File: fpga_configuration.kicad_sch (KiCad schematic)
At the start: 53 parts, among them IC1 ECP5-BGA256, J10 TC_SWD, J6 MCU_SWD, U6 ATSAMD11, U7 W25Q32JVSS

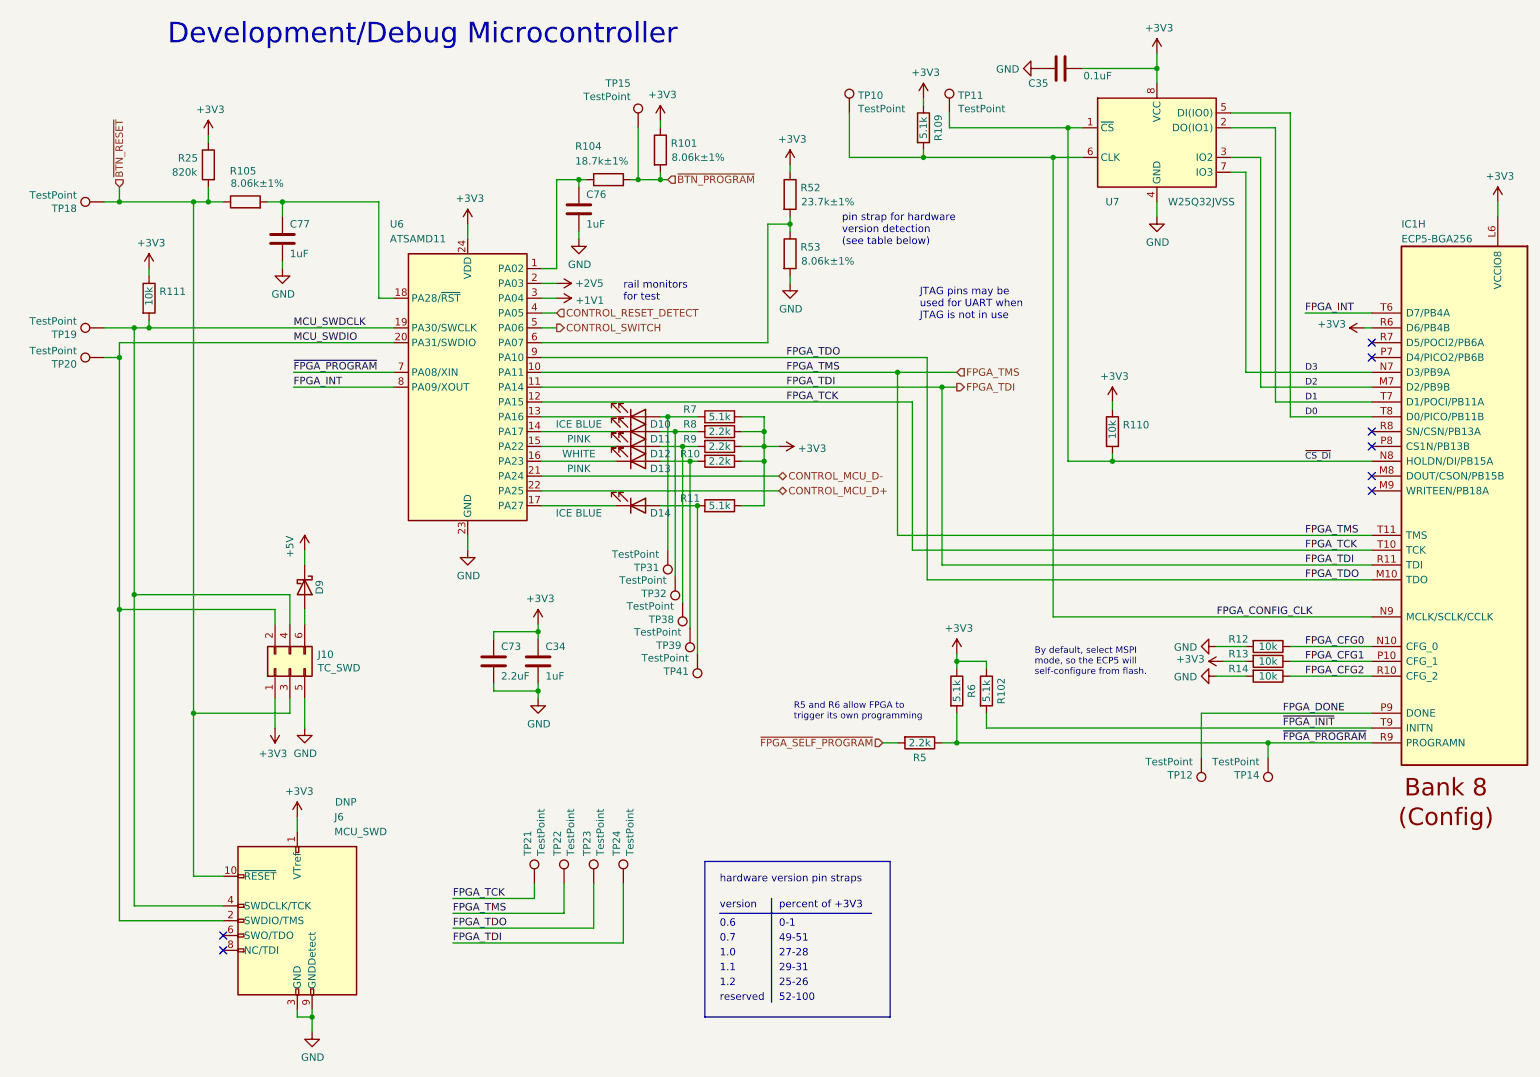
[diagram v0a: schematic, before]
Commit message: Connect FPGA_DONE and FPGA_INIT to microcontroller
Also pull FPGA_INIT (INITN) down instead of up. This prevents the FPGA
from self-configuring at start-up until the microcontroller drives the
signal high.

Connecting these signals give the microcontroller better control and
monitoring of the FPGA's configuration process.

To make room for these signals, the +1V1 and +2V5 measurement
connections are removed from the microcontroller.
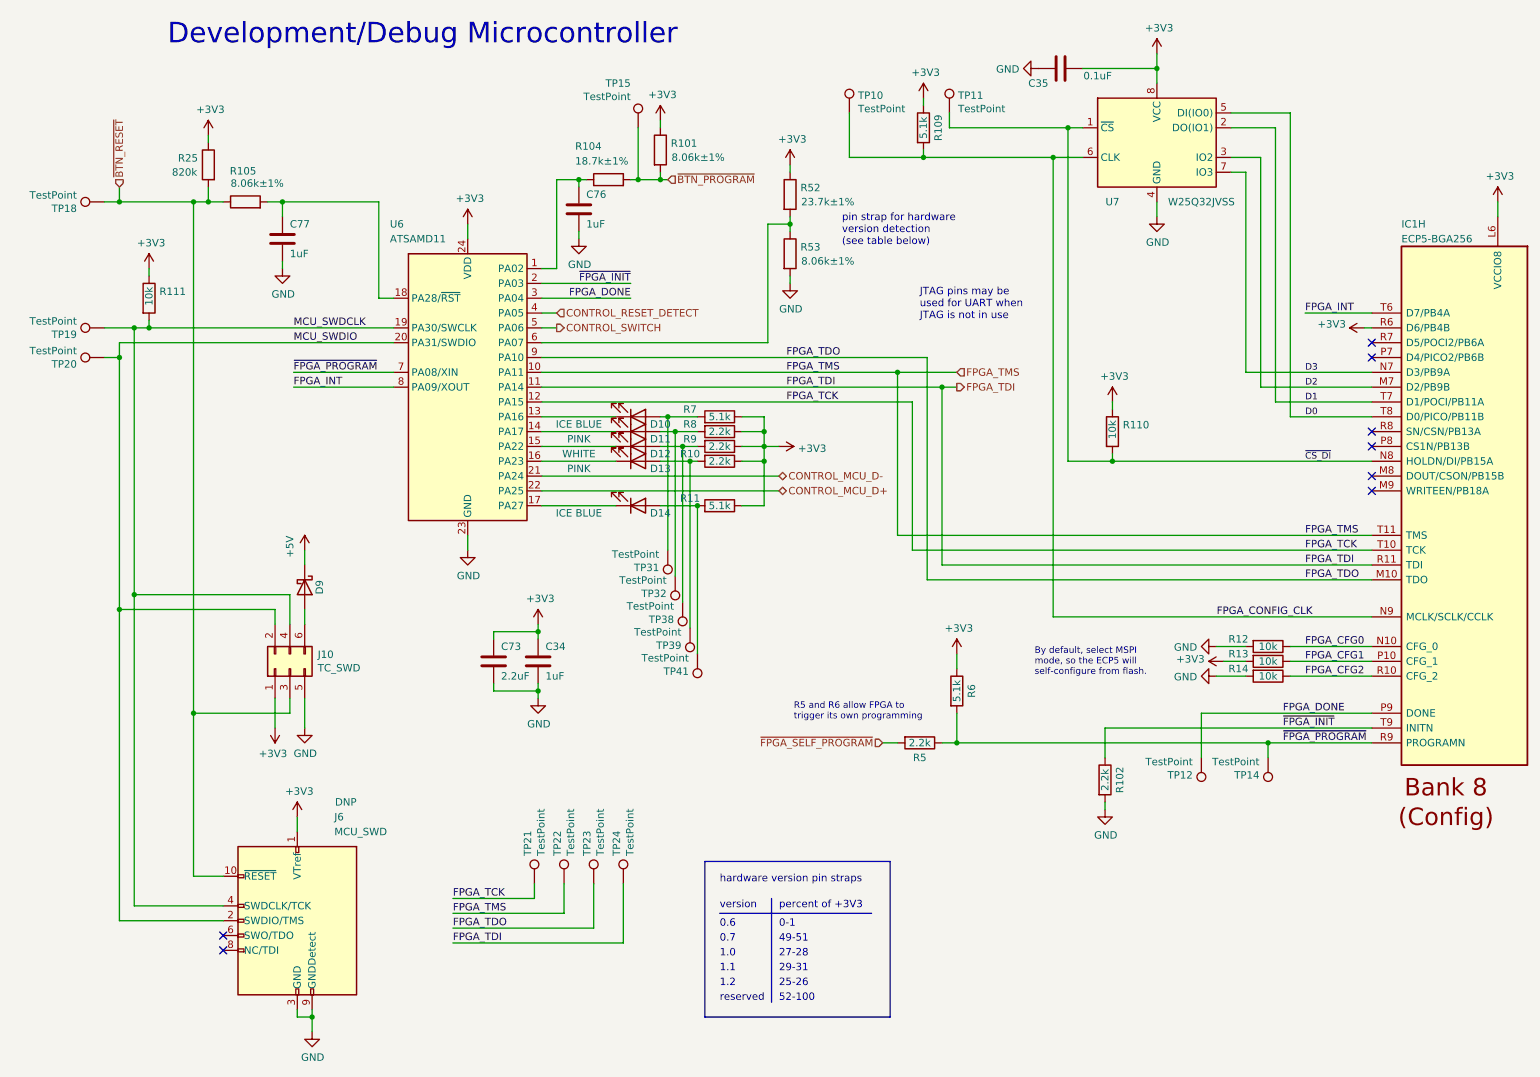
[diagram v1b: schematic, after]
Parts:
- R102: value 5.1k -> 2.2k; Part Number RC0402JR-075K1L -> RC0402JR-072K2L
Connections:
- net +1V1 is gone; now on net FPGA_DONE: U6.3 (PA04)
- net +2V5 is gone; now on net ~{FPGA_INIT}: U6.2 (PA03)
- net +3V3: no longer R102.1
- net GND: now also R102.2
- net ~{FPGA_INIT}: now also R102.1; no longer R102.2
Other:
- note removed: "rail monitors for test"
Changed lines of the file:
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@@
   (junction (at 33.02 74.93) (diameter 0) (color 0 0 0 0)
-  )
-  (junction (at 176.53 127) (diameter 0) (color 0 0 0 0)
   )
   (junction (at 121.92 44.45) (diameter 0) (color 0 0 0 0)
@@
     (stroke (width 0) (type default) (color 0 0 0 0))
   )
+  (wire (pts (xy 247.65 138.43) (xy 201.93 138.43))
+    (stroke (width 0) (type default) (color 0 0 0 0))
+  )
   (wire (pts (xy 107.95 69.85) (xy 105.41 69.85))
     (stroke (width 0) (type default) (color 0 0 0 0))
@@
     (stroke (width 0) (type default) (color 0 0 0 0))
   )
-  (wire (pts (xy 107.95 64.77) (xy 105.41 64.77))
+  (wire (pts (xy 120.65 64.77) (xy 105.41 64.77))
     (stroke (width 0) (type default) (color 0 0 0 0))
   )
@@
     (stroke (width 0) (type default) (color 0 0 0 0))
   )
-  (wire (pts (xy 176.53 125.73) (xy 176.53 127))
+  (wire (pts (xy 176.53 125.73) (xy 176.53 128.27))
     (stroke (width 0) (type default) (color 0 0 0 0))
   )
@@
     (stroke (width 0) (type default) (color 0 0 0 0))
   )
-  (wire (pts (xy 105.41 62.23) (xy 107.95 62.23))
+  (wire (pts (xy 105.41 62.23) (xy 120.65 62.23))
     (stroke (width 0) (type default) (color 0 0 0 0))
   )
@@
     (stroke (width 0) (type default) (color 0 0 0 0))
   )
+  (wire (pts (xy 201.93 151.13) (xy 201.93 152.4))
+    (stroke (width 0) (type default) (color 0 0 0 0))
+  )
   (wire (pts (xy 121.92 35.56) (xy 121.92 44.45))
     (stroke (width 0) (type default) (color 0 0 0 0))
@@
     (stroke (width 0) (type default) (color 0 0 0 0))
   )
-  (wire (pts (xy 181.61 135.89) (xy 181.61 138.43))
-    (stroke (width 0) (type default) (color 0 0 0 0))
-  )
   (wire (pts (xy 107.95 44.45) (xy 107.95 59.69))
     (stroke (width 0) (type default) (color 0 0 0 0))
@@
     (stroke (width 0) (type default) (color 0 0 0 0))
   )
-  (wire (pts (xy 176.53 127) (xy 176.53 128.27))
-    (stroke (width 0) (type default) (color 0 0 0 0))
-  )
   (wire (pts (xy 127 85.09) (xy 132.08 85.09))
     (stroke (width 0) (type default) (color 0 0 0 0))
@@
     (stroke (width 0) (type default) (color 0 0 0 0))
   )
-  (wire (pts (xy 247.65 138.43) (xy 181.61 138.43))
-    (stroke (width 0) (type default) (color 0 0 0 0))
-  )
   (wire (pts (xy 147.955 53.34) (xy 147.955 52.07))
     (stroke (width 0) (type default) (color 0 0 0 0))
   )
-  (wire (pts (xy 181.61 127) (xy 181.61 128.27))
-    (stroke (width 0) (type default) (color 0 0 0 0))
-  )
   (wire (pts (xy 109.22 170.18) (xy 90.17 170.18))
     (stroke (width 0) (type default) (color 0 0 0 0))
@@
     (stroke (width 0) (type default) (color 0 0 0 0))
   )
-  (wire (pts (xy 176.53 127) (xy 181.61 127))
-    (stroke (width 0) (type default) (color 0 0 0 0))
-  )
   (wire (pts (xy 63.5 187.96) (xy 66.04 187.96))
     (stroke (width 0) (type default) (color 0 0 0 0))
@@
   )
   (wire (pts (xy 50.8 48.26) (xy 48.26 48.26))
+    (stroke (width 0) (type default) (color 0 0 0 0))
+  )
+  (wire (pts (xy 201.93 138.43) (xy 201.93 143.51))
     (stroke (width 0) (type default) (color 0 0 0 0))
   )
@@
     (effects (font (size 1.27 1.27)) (justify left bottom))
   )
-  (text "rail monitors\nfor test" (at 119.38 65.405 0)
-    (effects (font (size 1.27 1.27)) (justify left bottom))
-  )
   (text "pin strap for hardware\nversion detection\n(see table below)"
     (at 156.845 55.88 0)
@@
     (effects (font (size 1.27 1.27)) (justify left bottom))
   )
+  (label "FPGA_DONE" (at 120.65 64.77 180)
+    (effects (font (size 1.27 1.27)) (justify right bottom))
+  )
   (label "MCU_SWDCLK" (at 62.865 69.85 0)
     (effects (font (size 1.27 1.27)) (justify left bottom))
+  )
+  (label "~{FPGA_INIT}" (at 120.65 62.23 180)
+    (effects (font (size 1.27 1.27)) (justify right bottom))
   )
   (label "FPGA_INT" (at 236.22 67.31 0)
@@
     )
     (property "Datasheet" "" (id 3) (at 146.05 90.17 0)
-      (effects (font (size 1.27 1.27)) hide)
-    )
-    (pin "1")
-  )
-  (symbol (lib_id "power:+1V1") (at 107.95 64.77 270) (unit 1)
-    (in_bom yes) (on_board yes)
-    (property "Reference" "#PWR040" (id 0) (at 104.14 64.77 0)
-      (effects (font (size 1.27 1.27)) hide)
-    )
-    (property "Value" "+1V1" (id 1) (at 111.2012 65.151 90)
-      (effects (font (size 1.27 1.27)) (justify left))
-    )
-    (property "Footprint" "" (id 2) (at 107.95 64.77 0)
-      (effects (font (size 1.27 1.27)) hide)
-    )
-    (property "Datasheet" "" (id 3) (at 107.95 64.77 0)
-      (effects (font (size 1.27 1.27)) hide)
-    )
-    (pin "1")
-  )
-  (symbol (lib_id "power:+2V5") (at 107.95 62.23 270) (unit 1)
-    (in_bom yes) (on_board yes)
-    (property "Reference" "#PWR046" (id 0) (at 104.14 62.23 0)
-      (effects (font (size 1.27 1.27)) hide)
-    )
-    (property "Value" "+2V5" (id 1) (at 111.125 62.23 90)
-      (effects (font (size 1.27 1.27)) (justify left))
-    )
-    (property "Footprint" "" (id 2) (at 107.95 62.23 0)
-      (effects (font (size 1.27 1.27)) hide)
-    )
-    (property "Datasheet" "" (id 3) (at 107.95 62.23 0)
       (effects (font (size 1.27 1.27)) hide)
     )
@@
     (pin "1")
   )
+  (symbol (lib_id "Device:R") (at 201.93 147.32 0) (unit 1)
+    (in_bom yes) (on_board yes)
+    (property "Reference" "R102" (id 0) (at 204.47 147.32 90))
+    (property "Value" "2.2k" (id 1) (at 201.93 147.32 90))
+    (property "Footprint" "Resistor_SMD:R_0402_1005Metric" (id 2) (at 200.152 147.32 90)
+      (effects (font (size 1.27 1.27)) hide)
+    )
+    (property "Datasheet" "~" (id 3) (at 201.93 147.32 0)
+      (effects (font (size 1.27 1.27)) hide)
+    )
+    (property "Part Number" "RC0402JR-072K2L" (id 4) (at 201.93 147.32 0)
+      (effects (font (size 1.27 1.27)) hide)
+    )
+    (property "Substitution" "any equivalent" (id 5) (at 201.93 147.32 0)
+      (effects (font (size 1.27 1.27)) hide)
+    )
+    (property "Description" "RES 2.2K OHM 5% 1/16W 0402" (id 6) (at 201.93 147.32 0)
+      (effects (font (size 1.27 1.27)) hide)
+    )
+    (property "Manufacturer" "Yageo" (id 7) (at 201.93 147.32 0)
+      (effects (font (size 1.27 1.27)) hide)
+    )
+    (pin "1")
+    (pin "2")
+  )
   (symbol (lib_id "Connector:TestPoint") (at 132.08 125.73 180) (unit 1)
     (in_bom no) (on_board yes)
@@
     (pin "2")
   )
+  (symbol (lib_id "power:GND") (at 201.93 152.4 0) (unit 1)
+    (in_bom yes) (on_board yes)
+    (property "Reference" "#PWR0237" (id 0) (at 201.93 158.75 0)
+      (effects (font (size 1.27 1.27)) hide)
+    )
+    (property "Value" "GND" (id 1) (at 202.057 156.7942 0))
+    (property "Footprint" "" (id 2) (at 201.93 152.4 0)
+      (effects (font (size 1.27 1.27)) hide)
+    )
+    (property "Datasheet" "" (id 3) (at 201.93 152.4 0)
+      (effects (font (size 1.27 1.27)) hide)
+    )
+    (pin "1")
+  )
   (symbol (lib_id "Device:R") (at 203.2 87.63 0) (unit 1)
     (in_bom yes) (on_board yes)
@@
     (pin "1")
   )
-  (symbol (lib_id "Device:R") (at 181.61 132.08 0) (unit 1)
-    (in_bom yes) (on_board yes)
-    (property "Reference" "R102" (id 0) (at 184.15 132.08 90))
-    (property "Value" "5.1k" (id 1) (at 181.61 132.08 90))
-    (property "Footprint" "Resistor_SMD:R_0402_1005Metric" (id 2) (at 179.832 132.08 90)
-      (effects (font (size 1.27 1.27)) hide)
-    )
-    (property "Datasheet" "~" (id 3) (at 181.61 132.08 0)
-      (effects (font (size 1.27 1.27)) hide)
-    )
-    (property "Part Number" "RC0402JR-075K1L" (id 4) (at 181.61 132.08 0)
-      (effects (font (size 1.27 1.27)) hide)
-    )
-    (property "Substitution" "any equivalent" (id 5) (at 181.61 132.08 0)
-      (effects (font (size 1.27 1.27)) hide)
-    )
-    (property "Description" "RES 5.1K OHM 5% 1/16W 0402" (id 6) (at 181.61 132.08 0)
-      (effects (font (size 1.27 1.27)) hide)
-    )
-    (property "Manufacturer" "Yageo" (id 7) (at 181.61 132.08 0)
-      (effects (font (size 1.27 1.27)) hide)
-    )
-    (pin "1")
-    (pin "2")
-  )
 )

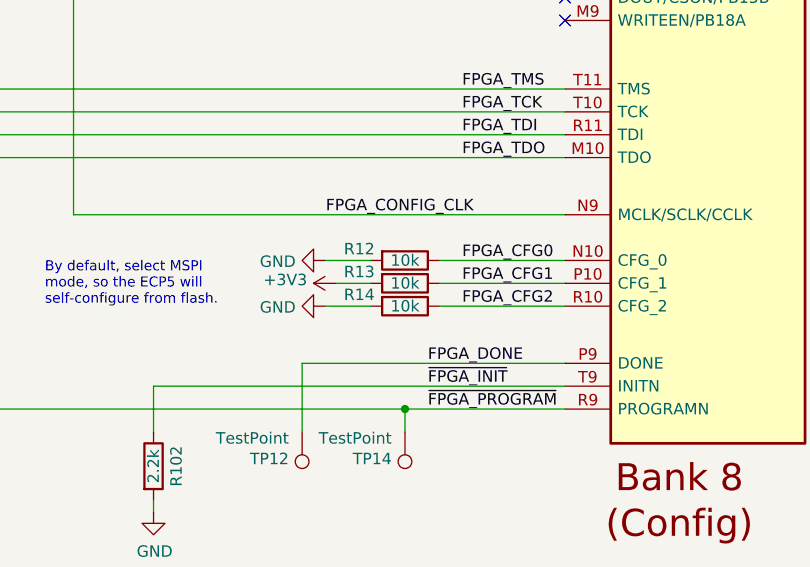
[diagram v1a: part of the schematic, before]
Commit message: Update CFG pull-up and pull-down resistor values
FPGA-TN-02039 says that 4.7k is recommended for pull-ups and that
pull-downs should be less than 500 ohms.

FPGA-TN-02038 says that pull-ups can be from 1k to 10k but is unclear on
pull-downs. Perhaps it is trying to suggest that pull-downs should be 0
ohms.

We've been using 10k for both pull-downs and pull-ups. We haven't
observed any configuration failures, but the pull-downs are clearly not
as effective as they could be, pulling the signals down to 1 V.

This changes pull-ups from 10k to 5.1k and pull-downs from 10k to 330
ohms.
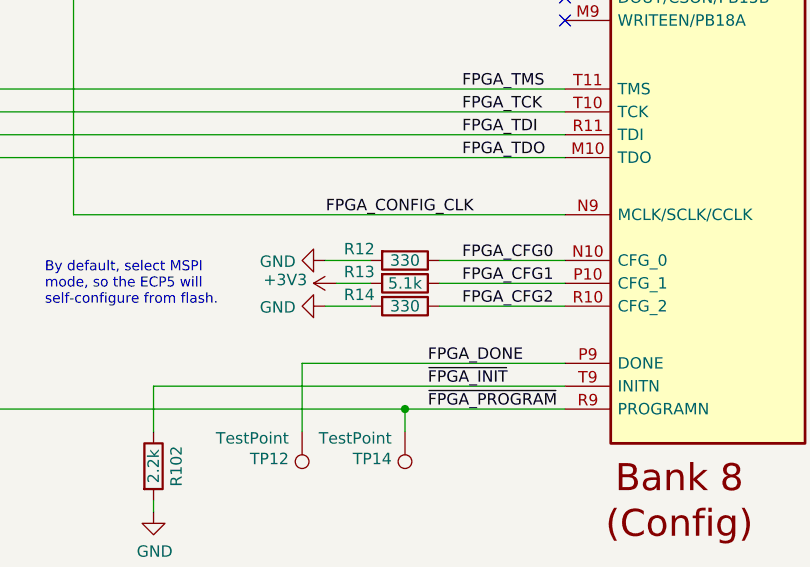
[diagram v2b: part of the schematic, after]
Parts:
- R12, R14: value 10k -> 330; Part Number RC0402JR-0710KL -> RC0402FR-13330RL
- R13: value 10k -> 5.1k; Part Number RC0402JR-0710KL -> RC0402JR-075K1L
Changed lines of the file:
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@@
     (in_bom yes) (on_board yes)
     (property "Reference" "R12" (id 0) (at 224.79 123.19 90))
-    (property "Value" "10k" (id 1) (at 229.87 124.46 90))
+    (property "Value" "330" (id 1) (at 229.87 124.46 90))
     (property "Footprint" "Resistor_SMD:R_0402_1005Metric" (id 2) (at 229.87 122.682 90)
       (effects (font (size 1.27 1.27)) hide)
@@
       (effects (font (size 1.27 1.27)) hide)
     )
-    (property "Part Number" "RC0402JR-0710KL" (id 4) (at 229.87 124.46 0)
+    (property "Part Number" "RC0402FR-13330RL" (id 4) (at 229.87 124.46 0)
       (effects (font (size 1.27 1.27)) hide)
     )
@@
       (effects (font (size 1.27 1.27)) hide)
     )
-    (property "Description" "RES 10K OHM 5% 1/16W 0402" (id 6) (at 229.87 124.46 0)
+    (property "Description" "RES 330 OHM 1% 1/16W 0402" (id 6) (at 229.87 124.46 0)
       (effects (font (size 1.27 1.27)) hide)
     )
@@
     (in_bom yes) (on_board yes)
     (property "Reference" "R13" (id 0) (at 224.79 125.73 90))
-    (property "Value" "10k" (id 1) (at 229.87 127 90))
+    (property "Value" "5.1k" (id 1) (at 229.87 127 90))
     (property "Footprint" "Resistor_SMD:R_0402_1005Metric" (id 2) (at 229.87 125.222 90)
       (effects (font (size 1.27 1.27)) hide)
@@
       (effects (font (size 1.27 1.27)) hide)
     )
-    (property "Part Number" "RC0402JR-0710KL" (id 4) (at 229.87 127 0)
+    (property "Part Number" "RC0402JR-075K1L" (id 4) (at 229.87 127 0)
       (effects (font (size 1.27 1.27)) hide)
     )
@@
       (effects (font (size 1.27 1.27)) hide)
     )
-    (property "Description" "RES 10K OHM 5% 1/16W 0402" (id 6) (at 229.87 127 0)
+    (property "Description" "RES 5.1K OHM 5% 1/16W 0402" (id 6) (at 229.87 127 0)
       (effects (font (size 1.27 1.27)) hide)
     )
@@
     (in_bom yes) (on_board yes)
     (property "Reference" "R14" (id 0) (at 224.79 128.27 90))
-    (property "Value" "10k" (id 1) (at 229.87 129.54 90))
+    (property "Value" "330" (id 1) (at 229.87 129.54 90))
     (property "Footprint" "Resistor_SMD:R_0402_1005Metric" (id 2) (at 229.87 127.762 90)
       (effects (font (size 1.27 1.27)) hide)
@@
       (effects (font (size 1.27 1.27)) hide)
     )
-    (property "Part Number" "RC0402JR-0710KL" (id 4) (at 229.87 129.54 0)
+    (property "Part Number" "RC0402FR-13330RL" (id 4) (at 229.87 129.54 0)
       (effects (font (size 1.27 1.27)) hide)
     )
@@
       (effects (font (size 1.27 1.27)) hide)
     )
-    (property "Description" "RES 10K OHM 5% 1/16W 0402" (id 6) (at 229.87 129.54 0)
+    (property "Description" "RES 330 OHM 1% 1/16W 0402" (id 6) (at 229.87 129.54 0)
       (effects (font (size 1.27 1.27)) hide)
     )
